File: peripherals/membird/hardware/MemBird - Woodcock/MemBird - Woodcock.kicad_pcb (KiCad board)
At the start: 2 copper layers, 100 x 100 mm, 3 parts, among them U3 VME64-P1-3R

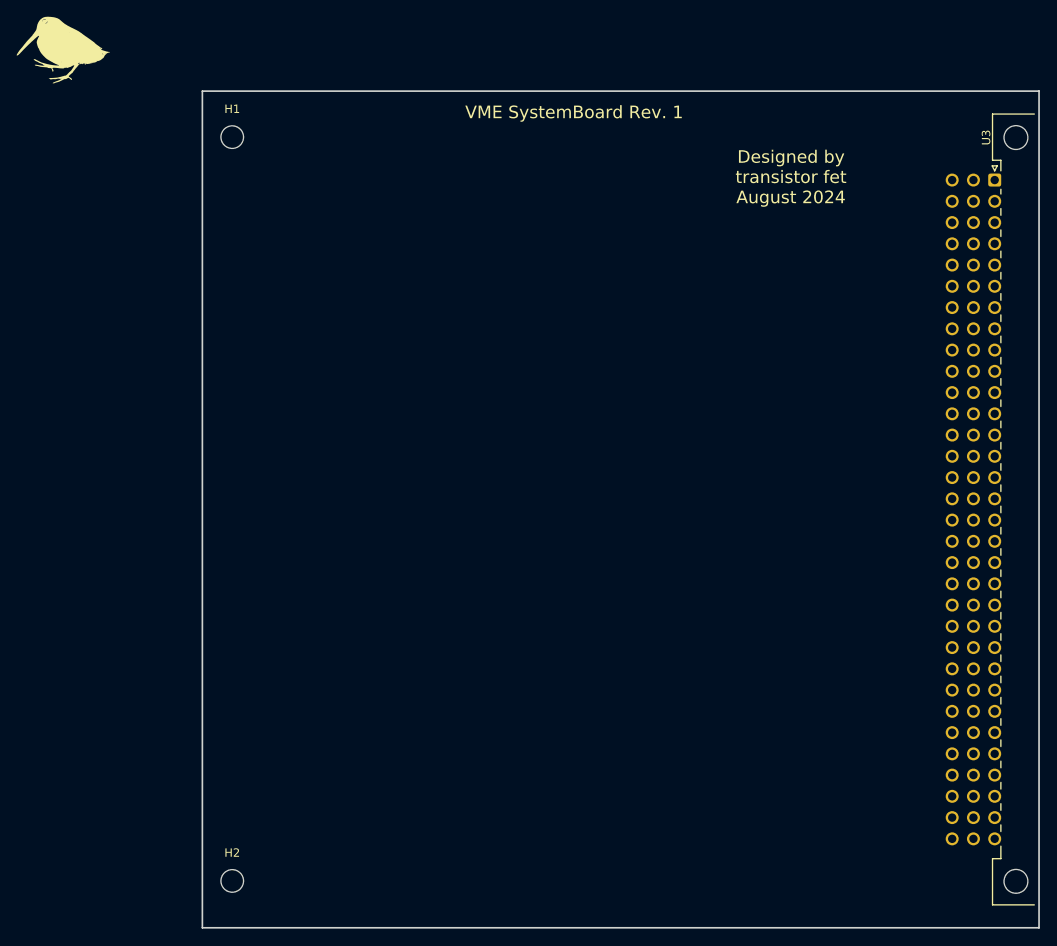
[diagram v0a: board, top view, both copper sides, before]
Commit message: Finished the MemBird - Woodcock 16-bit memory board layout
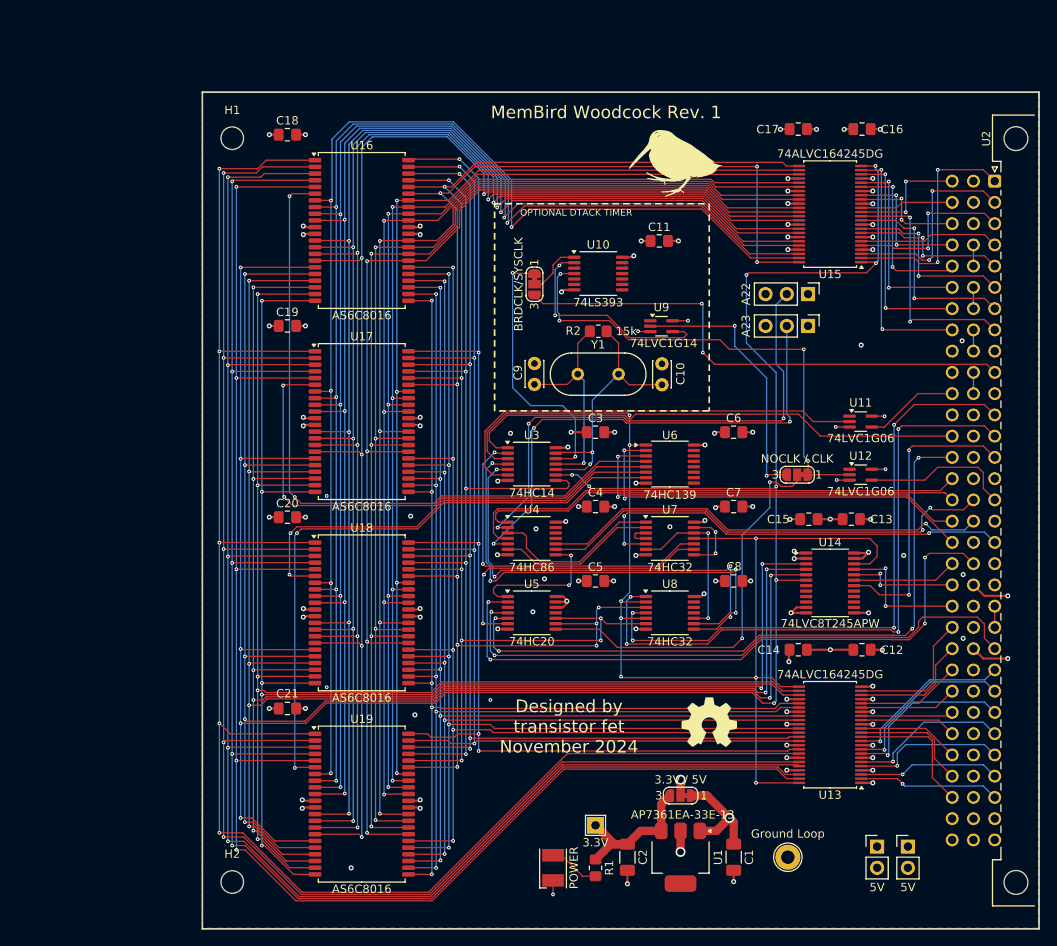
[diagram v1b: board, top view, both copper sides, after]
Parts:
- added C1: 4.7uF, Capacitor_SMD:C_1206_3216Metric_Pad1.33x1.80mm_HandSolder, F.Cu at (101.6, 116.8)
- added C10: 18pF, Capacitor_THT:C_Disc_D3.0mm_W2.0mm_P2.50mm, F.Cu at (93.0, 60.4)
- added C11: 0.1uF, Capacitor_SMD:C_0805_2012Metric_Pad1.18x1.45mm_HandSolder, F.Cu at (92.7, 43.2)
- added C12: 0.1uF, Capacitor_SMD:C_0805_2012Metric_Pad1.18x1.45mm_HandSolder, F.Cu at (116.9, 92.0)
- added C13: 0.1uF, Capacitor_SMD:C_0805_2012Metric_Pad1.18x1.45mm_HandSolder, F.Cu at (115.7, 76.4)
- added C14: 0.1uF, Capacitor_SMD:C_0805_2012Metric_Pad1.18x1.45mm_HandSolder, F.Cu at (109.3, 92.0)
- added C15: 0.1uF, Capacitor_SMD:C_0805_2012Metric_Pad1.18x1.45mm_HandSolder, F.Cu at (110.6, 76.4)
- added C16: 0.1uF, Capacitor_SMD:C_0805_2012Metric_Pad1.18x1.45mm_HandSolder, F.Cu at (116.9, 29.8)
- added C17: 0.1uF, Capacitor_SMD:C_0805_2012Metric_Pad1.18x1.45mm_HandSolder, F.Cu at (109.3, 29.8)
- added C18: 0.1uF, Capacitor_SMD:C_0805_2012Metric_Pad1.18x1.45mm_HandSolder, F.Cu at (48.3, 30.5)
- added C19: 0.1uF, Capacitor_SMD:C_0805_2012Metric_Pad1.18x1.45mm_HandSolder, F.Cu at (48.3, 53.3)
- added C2: 4.7uF, Capacitor_SMD:C_1206_3216Metric_Pad1.33x1.80mm_HandSolder, F.Cu at (88.9, 116.8)
- added C20: 0.1uF, Capacitor_SMD:C_0805_2012Metric_Pad1.18x1.45mm_HandSolder, F.Cu at (48.3, 76.2)
- added C21: 0.1uF, Capacitor_SMD:C_0805_2012Metric_Pad1.18x1.45mm_HandSolder, F.Cu at (48.3, 99.1)
- added C3: 0.1uF, Capacitor_SMD:C_0805_2012Metric_Pad1.18x1.45mm_HandSolder, F.Cu at (85.1, 66.0)
- added C4: 0.1uF, Capacitor_SMD:C_0805_2012Metric_Pad1.18x1.45mm_HandSolder, F.Cu at (85.1, 74.9)
- added C5: 0.1uF, Capacitor_SMD:C_0805_2012Metric_Pad1.18x1.45mm_HandSolder, F.Cu at (85.1, 83.8)
- added C6: 0.1uF, Capacitor_SMD:C_0805_2012Metric_Pad1.18x1.45mm_HandSolder, F.Cu at (101.6, 66.0)
- added C7: 0.1uF, Capacitor_SMD:C_0805_2012Metric_Pad1.18x1.45mm_HandSolder, F.Cu at (101.6, 74.9)
- added C8: 0.1uF, Capacitor_SMD:C_0805_2012Metric_Pad1.18x1.45mm_HandSolder, F.Cu at (101.6, 83.8)
- added C9: 18pF, Capacitor_THT:C_Disc_D3.0mm_W2.0mm_P2.50mm, F.Cu at (77.8, 60.3)
- added D1: POWER, LED_SMD:LED_PLCC-2_3.4x3.0mm_KA, F.Cu at (80.0, 118.1)
- added J2: 5V, Connector_PinHeader_2.54mm:PinHeader_1x02_P2.54mm_Vertical, F.Cu at (118.7, 115.6)
- added J3: 5V, Connector_PinHeader_2.54mm:PinHeader_1x02_P2.54mm_Vertical, F.Cu at (122.4, 115.6)
- added JP1: 3.3V / 5V, Jumper:SolderJumper-3_P1.3mm_Bridged12_RoundedPad1.0x1.5mm_NumberLabels, F.Cu at (95.2, 109.5)
- added JP2: A23, Connector_PinHeader_2.54mm:PinHeader_1x03_P2.54mm_Vertical, F.Cu at (110.5, 53.3)
- added JP3: A22, Connector_PinHeader_2.54mm:PinHeader_1x03_P2.54mm_Vertical, F.Cu at (110.5, 49.5)
- added JP4: NOCLK / CLK, Jumper:SolderJumper-3_P1.3mm_Bridged12_RoundedPad1.0x1.5mm_NumberLabels, F.Cu at (109.2, 71.1)
- added JP5: BRDCLK/SYSCLK, Jumper:SolderJumper-3_P1.3mm_Bridged12_RoundedPad1.0x1.5mm_NumberLabels, F.Cu at (77.8, 48.4)
- added R1: 220, Resistor_SMD:R_0805_2012Metric_Pad1.20x1.40mm_HandSolder, F.Cu at (85.1, 118.1)
- added R2: 15k, Resistor_SMD:R_0805_2012Metric_Pad1.20x1.40mm_HandSolder, F.Cu at (85.4, 54.0)
- added S1: Logo_Open_Hardware_Small, Symbol:OSHW-Symbol_6.7x6mm_SilkScreen, F.Cu at (98.7, 100.7)
- added TP1: Ground Loop, TestPoint:TestPoint_Loop_D2.60mm_Drill1.6mm_Beaded, F.Cu at (108.1, 116.8)
- added TP2: 3.3V, TestPoint:TestPoint_THTPad_2.0x2.0mm_Drill1.0mm, F.Cu at (85.1, 113.0)
- added U1: AP7361EA-33E-13, Package_TO_SOT_SMD:SOT-223, F.Cu at (95.2, 116.8)
- added U10: 74LS393, Package_SO:TSSOP-14_4.4x5mm_P0.65mm, F.Cu at (85.4, 47.1)
- added U11: 74LVC1G06, Package_TO_SOT_SMD:SOT-353_SC-70-5_Handsoldering, F.Cu at (116.8, 64.8)
- added U12: 74LVC1G06, Package_TO_SOT_SMD:SOT-353_SC-70-5_Handsoldering, F.Cu at (116.8, 71.1)
- added U13: 74ALVC164245DG, Package_SO:TSSOP-48_6.1x12.5mm_P0.5mm, F.Cu at (113.1, 102.2)
- added U14: 74LVC8T245APW, Package_SO:TSSOP-24_4.4x7.8mm_P0.65mm, F.Cu at (113.1, 84.1)
- added U15: 74ALVC164245DG, Package_SO:TSSOP-48_6.1x12.5mm_P0.5mm, F.Cu at (113.1, 40.0)
- added U16: AS6C8016, Package_SO:TSOP-II-44_10.16x18.41mm_P0.8mm, F.Cu at (57.1, 41.9)
- added U17: AS6C8016, Package_SO:TSOP-II-44_10.16x18.41mm_P0.8mm, F.Cu at (57.1, 64.8)
- added U18: AS6C8016, Package_SO:TSOP-II-44_10.16x18.41mm_P0.8mm, F.Cu at (57.1, 87.6)
- added U19: AS6C8016, Package_SO:TSOP-II-44_10.16x18.41mm_P0.8mm, F.Cu at (57.1, 110.5)
- added U3: 74HC14, Package_SO:TSSOP-14_4.4x5mm_P0.65mm, F.Cu at (77.5, 69.8)
- added U4: 74HC86, Package_SO:TSSOP-14_4.4x5mm_P0.65mm, F.Cu at (77.5, 78.7)
- added U5: 74HC20, Package_SO:TSSOP-14_4.4x5mm_P0.65mm, F.Cu at (77.5, 87.6)
- added U6: 74HC139, Package_SO:TSSOP-16_4.4x5mm_P0.65mm, F.Cu at (94.0, 69.8)
- added U7: 74HC32, Package_SO:TSSOP-14_4.4x5mm_P0.65mm, F.Cu at (94.0, 78.7)
- added U8: 74HC32, Package_SO:TSSOP-14_4.4x5mm_P0.65mm, F.Cu at (94.0, 87.6)
- added U9: 74LVC1G14, Package_TO_SOT_SMD:SOT-353_SC-70-5_Handsoldering, F.Cu at (93.0, 53.4)
- added Y1: Crystal, Crystal:Crystal_HC49-4H_Vertical, F.Cu at (83.0, 59.1)
- moved U2 0.13 mm to (132.8, 36.0)
- moved H1 0.13 mm to (41.7, 30.9)
- moved H2 0.13 mm to (41.7, 119.8)
- renumbered U3 to U2
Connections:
- U2 pad a1: (no net) -> VD0
- U2 pad a10: (no net) -> ~{SYSCLK}
- U2 pad a11: (no net) -> GND
- U2 pad a12: (no net) -> ~{VDS1}
- U2 pad a13: (no net) -> ~{VDS0}
- U2 pad a14: (no net) -> ~{VWRITE}
- U2 pad a15: (no net) -> GND
- U2 pad a16: (no net) -> ~{VDTACK}
- U2 pad a17: (no net) -> GND
- U2 pad a18: (no net) -> ~{VAS}
- U2 pad a19: (no net) -> GND
- U2 pad a2: (no net) -> VD1
- U2 pad a20: (no net) -> unconnected-(U2A-~{IACK}-Pada20)
- U2 pad a21: (no net) -> Net-(U2A-~{IACKIN})
- U2 pad a22: (no net) -> Net-(U2A-~{IACKIN})
- U2 pad a23: (no net) -> VAM4
- U2 pad a24: (no net) -> VA7
- U2 pad a25: (no net) -> VA6
- U2 pad a26: (no net) -> VA5
- U2 pad a27: (no net) -> VA4
- U2 pad a28: (no net) -> VA3
- U2 pad a29: (no net) -> VA2
- U2 pad a3: (no net) -> VD2
- U2 pad a30: (no net) -> VA1
- U2 pad a31: (no net) -> unconnected-(U2A--12V-Pada31)
- U2 pad a32: (no net) -> VBUS
- U2 pad a4: (no net) -> VD3
- U2 pad a5: (no net) -> VD4
- U2 pad a6: (no net) -> VD5
- U2 pad a7: (no net) -> VD6
- U2 pad a8: (no net) -> VD7
- U2 pad a9: (no net) -> GND
- U2 pad b1: (no net) -> unconnected-(U2B-~{BBSY}-Padb1)
- U2 pad b10: (no net) -> Net-(U2B-~{BG3IN})
- U2 pad b11: (no net) -> Net-(U2B-~{BG3IN})
- U2 pad b12: (no net) -> unconnected-(U2B-~{BR0}-Padb12)
- U2 pad b13: (no net) -> unconnected-(U2B-~{BR1}-Padb13)
- U2 pad b14: (no net) -> unconnected-(U2B-~{BR2}-Padb14)
- U2 pad b15: (no net) -> unconnected-(U2B-~{BR3}-Padb15)
- U2 pad b16: (no net) -> VAM0
- U2 pad b17: (no net) -> VAM1
- U2 pad b18: (no net) -> VAM2
- U2 pad b19: (no net) -> VAM3
- U2 pad b2: (no net) -> unconnected-(U2B-~{BCLR}-Padb2)
- U2 pad b20: (no net) -> GND
- U2 pad b21: (no net) -> unconnected-(U2B-SERCLK-Padb21)
- U2 pad b22: (no net) -> unconnected-(U2B-SERDAT-Padb22)
- U2 pad b23: (no net) -> GND
- U2 pad b24: (no net) -> unconnected-(U2B-~{IRQ7}-Padb24)
- U2 pad b25: (no net) -> unconnected-(U2B-~{IRQ6}-Padb25)
- U2 pad b26: (no net) -> unconnected-(U2B-~{IRQ5}-Padb26)
- U2 pad b27: (no net) -> unconnected-(U2B-~{IRQ4}-Padb27)
- U2 pad b28: (no net) -> unconnected-(U2B-~{IRQ3}-Padb28)
- U2 pad b29: (no net) -> unconnected-(U2B-~{IRQ2}-Padb29)
- U2 pad b3: (no net) -> unconnected-(U2B-~{ACFAIL}-Padb3)
- U2 pad b30: (no net) -> unconnected-(U2B-~{IRQ1}-Padb30)
- U2 pad b31: (no net) -> unconnected-(U2B-+5VStdby-Padb31)
- U2 pad b32: (no net) -> VBUS
- U2 pad b4: (no net) -> Net-(U2B-~{BG0IN})
- U2 pad b5: (no net) -> Net-(U2B-~{BG0IN})
- U2 pad b6: (no net) -> Net-(U2B-~{BG1IN})
- U2 pad b7: (no net) -> Net-(U2B-~{BG1IN})
- U2 pad b8: (no net) -> Net-(U2B-~{BG2IN})
- U2 pad b9: (no net) -> Net-(U2B-~{BG2IN})
- U2 pad c1: (no net) -> VD8
- U2 pad c10: (no net) -> unconnected-(U2C-~{SYSFAIL}-Padc10)
- U2 pad c11: (no net) -> ~{VBERR}
- U2 pad c12: (no net) -> unconnected-(U2C-~{SYSRESET}-Padc12)
- U2 pad c13: (no net) -> ~{VLWORD}
- U2 pad c14: (no net) -> VAM5
- U2 pad c15: (no net) -> VA23
- U2 pad c16: (no net) -> VA22
- U2 pad c17: (no net) -> VA21
- U2 pad c18: (no net) -> VA20
- U2 pad c19: (no net) -> VA19
- U2 pad c2: (no net) -> VD9
- U2 pad c20: (no net) -> VA18
- U2 pad c21: (no net) -> VA17
- U2 pad c22: (no net) -> VA16
- U2 pad c23: (no net) -> VA15
- U2 pad c24: (no net) -> VA14
- U2 pad c25: (no net) -> VA13
- U2 pad c26: (no net) -> VA12
- U2 pad c27: (no net) -> VA11
- U2 pad c28: (no net) -> VA10
- U2 pad c29: (no net) -> VA9
- U2 pad c3: (no net) -> VD10
- U2 pad c30: (no net) -> VA8
- U2 pad c31: (no net) -> unconnected-(U2C-+12V-Padc31)
- U2 pad c32: (no net) -> VBUS
- U2 pad c4: (no net) -> VD11
- U2 pad c5: (no net) -> VD12
- U2 pad c6: (no net) -> VD13
- U2 pad c7: (no net) -> VD14
- U2 pad c8: (no net) -> VD15
- U2 pad c9: (no net) -> GND
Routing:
- net ~{WR}: track 0.00 -> 283.4 mm, vias 0 -> 13
- net LA5: track 0.00 -> 205.1 mm, vias 0 -> 5
- net LA4: track 0.00 -> 201.7 mm, vias 0 -> 5
- net LA3: track 0.00 -> 198.9 mm, vias 0 -> 5
- net LA2: track 0.00 -> 196.4 mm, vias 0 -> 5
- net LA1: track 0.00 -> 193.6 mm, vias 0 -> 5
- net LA19: track 0.00 -> 184.0 mm, vias 0 -> 7
- net LA18: track 0.00 -> 180.4 mm, vias 0 -> 7
- net ~{LDS}: track 0.00 -> 178.4 mm, vias 0 -> 10
- net LA17: track 0.00 -> 177.6 mm, vias 0 -> 7
- net ~{UDS}: track 0.00 -> 166.9 mm, vias 0 -> 7
- net LD7: track 0.00 -> 163.7 mm, vias 0 -> 5
- net LD6: track 0.00 -> 161.6 mm, vias 0 -> 5
- net LD5: track 0.00 -> 160.3 mm, vias 0 -> 5
- net LA16: track 0.00 -> 159.8 mm, vias 0 -> 5
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- added copper zone on B.Cu, net GND
- added copper zone on F.Cu, net GND
- added copper zone on In2.Cu, net GND
- added copper zone on In1.Cu, net VBUS
- added copper zone on In1.Cu, net VMEM
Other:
- copper layers 2 -> 4
- board text added: "Designed by transistor fet November 2024"
- board text added: "MemBird Woodcock Rev. 1"
- board text added: "OPTIONAL DTACK TIMER"
- board text removed: "Designed by transistor fet August 2024"
- board text removed: "VME SystemBoard Rev. 1"

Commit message: k30p-VME rev.1, MemBird Woodcock rev.1, and frontpanels
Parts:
- added JP6: /2, Jumper:SolderJumper-2_P1.3mm_Open_RoundedPad1.0x1.5mm, F.Cu at (77.8, 46.4)
- added JP7: /4, Jumper:SolderJumper-2_P1.3mm_Bridged_RoundedPad1.0x1.5mm, F.Cu at (77.8, 48.9)
- added JP8: /8, Jumper:SolderJumper-2_P1.3mm_Open_RoundedPad1.0x1.5mm, F.Cu at (77.8, 51.4)
- added JP9: /16, Jumper:SolderJumper-2_P1.3mm_Open_RoundedPad1.0x1.5mm, F.Cu at (77.8, 54.0)
- D1: value POWER -> 3.3V POWER
- U10: value 74LS393 -> 74HC393
- moved JP5 5.99 mm to (78.6, 42.4), turned to 0 degrees
- moved C11 2.22 mm to (94.9, 43.2)
- moved U10 2.22 mm to (87.6, 47.1)
- moved D1 0.64 mm to (79.9, 118.7), turned to 0 degrees
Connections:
- U10 pad 3: unconnected-(U10A-Q0-Pad3) -> Net-(JP6-A)
- U10 pad 4: Net-(JP4-A) -> Net-(JP7-A)
- U10 pad 5: unconnected-(U10A-Q2-Pad5) -> Net-(JP8-A)
- U10 pad 6: unconnected-(U10A-Q3-Pad6) -> Net-(JP9-A)
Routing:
- net Net-(JP9-A): track 0.00 -> 9.85 mm
- net Net-(JP8-A): track 0.00 -> 7.82 mm
- net ~{SYSCLK}: track 62.2 -> 70.0 mm
- net Net-(JP7-A): track 0.00 -> 7.05 mm
- net Net-(JP4-A): track 58.3 -> 64.6 mm, vias 4 -> 2
- net Net-(JP6-A): track 0.00 -> 6.33 mm
- net Net-(JP5-A): track 32.4 -> 36.3 mm
- net Net-(U10A-MR): track 26.9 -> 29.8 mm
- net Net-(D1-A): track 6.12 -> 3.83 mm
- net +3.3V: track 18.6 -> 20.1 mm
- net Net-(JP5-C): track 6.66 -> 7.82 mm
- net Net-(C9-Pad1): track 25.8 -> 26.7 mm
